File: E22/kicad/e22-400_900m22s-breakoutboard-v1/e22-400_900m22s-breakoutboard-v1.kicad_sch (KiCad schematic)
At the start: 7 parts, among them IC1 E22-900M22S, U1 AMS1117-3.3

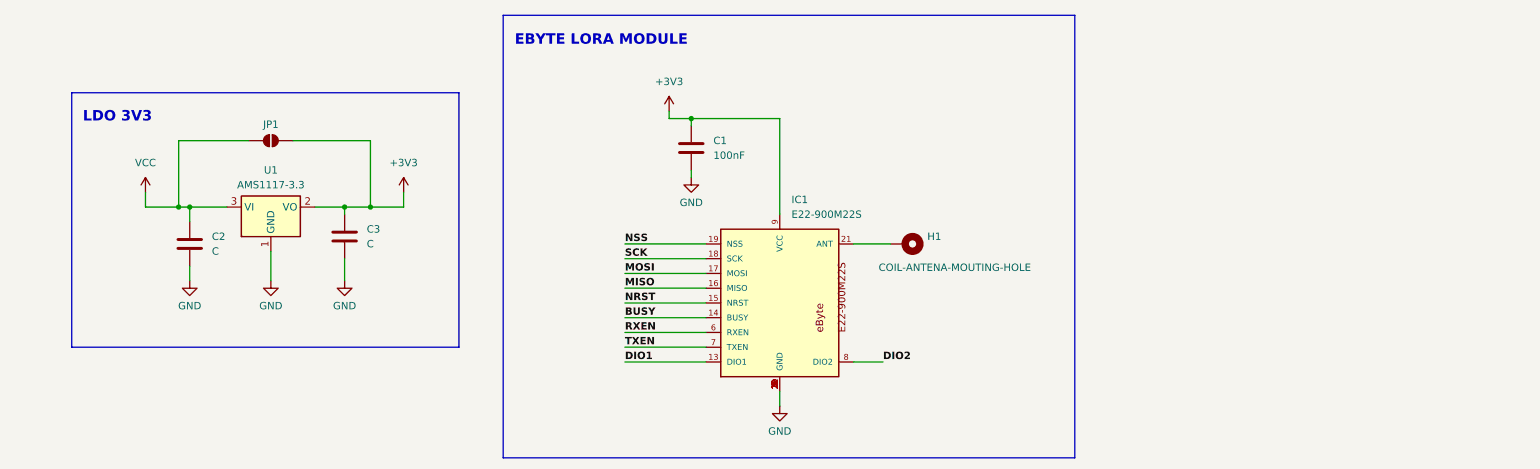
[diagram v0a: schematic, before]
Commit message: Update sch add breakout pins, reset button
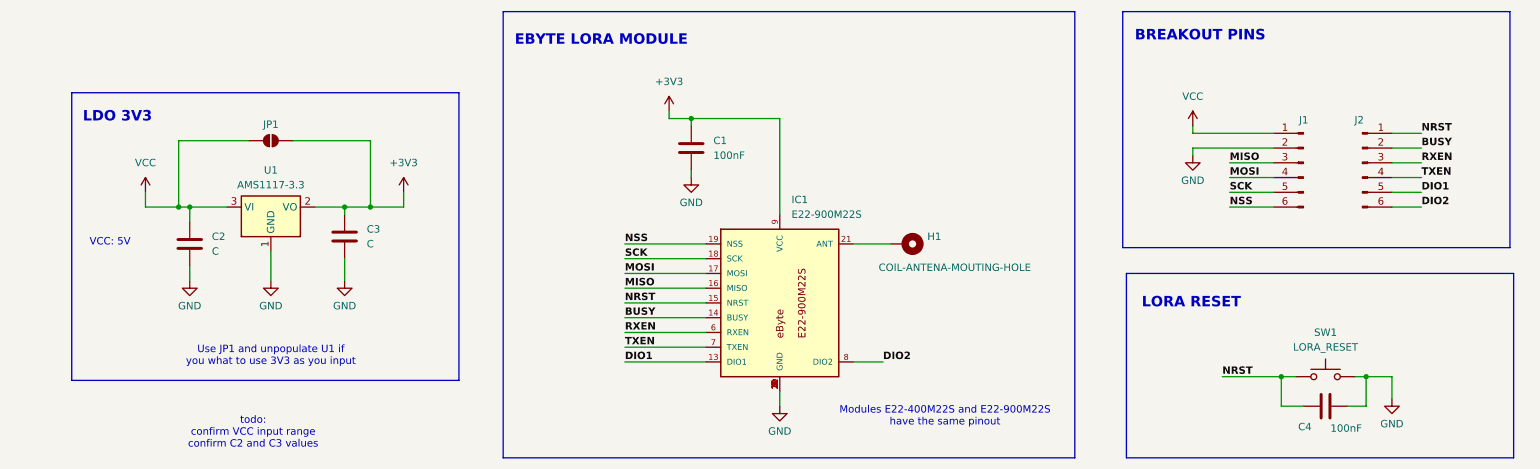
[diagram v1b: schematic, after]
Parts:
- added C4: 100nF, symbol Device:C
- added J1, J2: Conn_01x06_Pin, symbol Connector:Conn_01x06_Pin
- added SW1: LORA_RESET, symbol Switch:SW_Push
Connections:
- net BUSY: now also J2.2 (Pin_2)
- net DIO1: now also J2.5 (Pin_5)
- net DIO2: now also J2.6 (Pin_6)
- net GND: now also C4.1, J1.2 (Pin_2), SW1.2
- net MISO: now also J1.3 (Pin_3)
- net MOSI: now also J1.4 (Pin_4)
- net NRST: now also C4.2, J2.1 (Pin_1), SW1.1
- net NSS: now also J1.6 (Pin_6)
- net RXEN: now also J2.3 (Pin_3)
- net SCK: now also J1.5 (Pin_5)
- net TXEN: now also J2.4 (Pin_4)
- net VCC: now also J1.1 (Pin_1)
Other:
- note added: "BREAKOUT PINS"
- note added: "LORA RESET"
- note added: "Modules E22-400M22S and E22-900M22S have the same pinout"
- note added: "Use JP1 and unpopulate U1 if you what to use 3V3 as you input"
- note added: "VCC: 5V"
- note added: "todo: confirm VCC input range confirm C2 and C3 values"

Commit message: Update sch, values of caps LDO. Add res and led for power on.
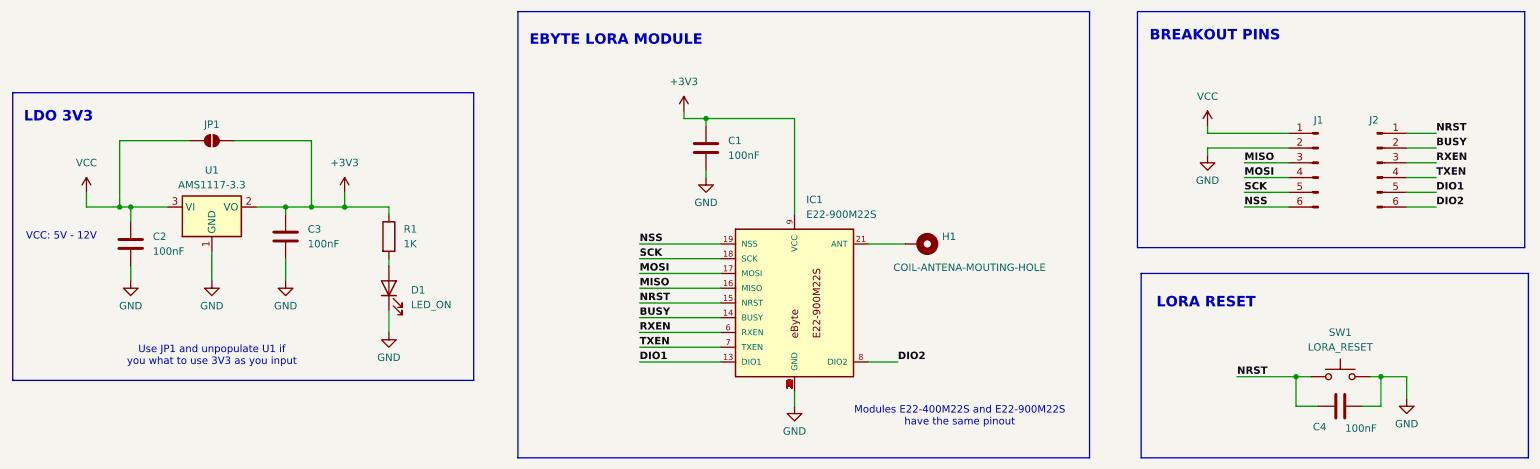
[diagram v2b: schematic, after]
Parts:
- added D1: LED_ON, LED_SMD:LED_0805_2012Metric_Pad1.15x1.40mm_HandSolder, symbol Device:LED
- added R1: 1K, Resistor_SMD:R_0805_2012Metric_Pad1.20x1.40mm_HandSolder, symbol Device:R
- C1, C4: footprint (none) -> Capacitor_SMD:C_0805_2012Metric_Pad1.18x1.45mm_HandSolder
- C2, C3: value C -> 100nF; footprint (none) -> Capacitor_SMD:C_0805_2012Metric_Pad1.18x1.45mm_HandSolder
- H1: footprint (none) -> MountingHole:MountingHole_2.2mm_M2_DIN965_Pad
- J1, J2: footprint (none) -> Connector_PinHeader_2.54mm:PinHeader_1x06_P2.54mm_Vertical
- JP1: footprint (none) -> Jumper:SolderJumper-2_P1.3mm_Open_TrianglePad1.0x1.5mm
- SW1: footprint (none) -> Button_Switch_SMD:SW_SPST_CK_RS282G05A3
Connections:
- net +3V3: now also R1.1
- net GND: now also D1.1 (K)
- new net: D1.2 (A), R1.2
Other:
- note added: "VCC: 5V - 12V"
- note removed: "VCC: 5V"
- note removed: "todo: confirm VCC input range confirm C2 and C3 values"
- moved on the sheet: C1, C2, C3, C4, H1, IC1, J1, J2, JP1, SW1, U1
